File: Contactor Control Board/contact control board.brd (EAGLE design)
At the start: 75.9 x 50.8 mm, 29 parts, among them K1 DS2Y-S-DC5V, Q1 2n2222, Q3 2n2222, Q4 MOSFET-NCHANNELFQP30N06L, U1 LM393AN

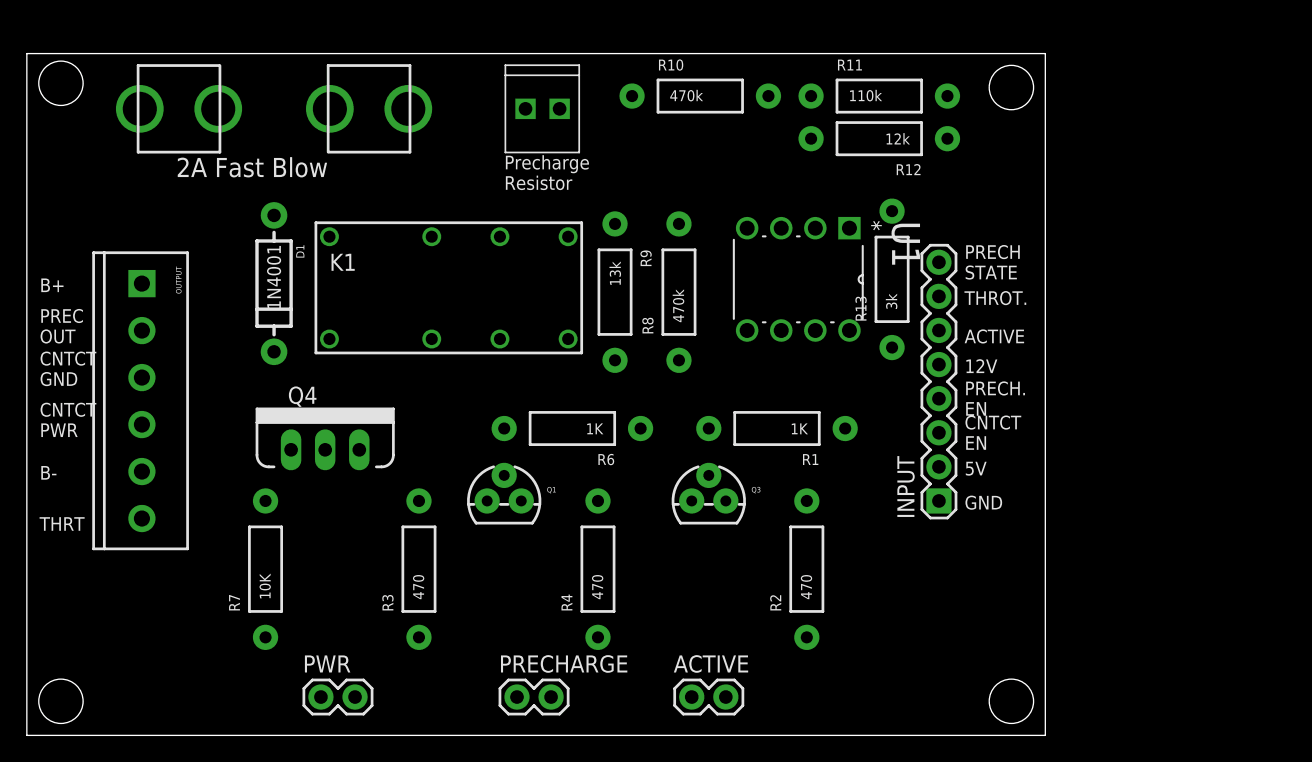
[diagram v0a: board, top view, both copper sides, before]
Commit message: Deleting SMD variant of the CCB for now.
Keeping the two boards in design sync while iterating on one wasn't a
smart idea. Conversion will happen once the CCB has been validated using
proto-boards. Did a test route of the CCB using thru-hole parts in a
2"x3" space and there's a ton of room. Cool!
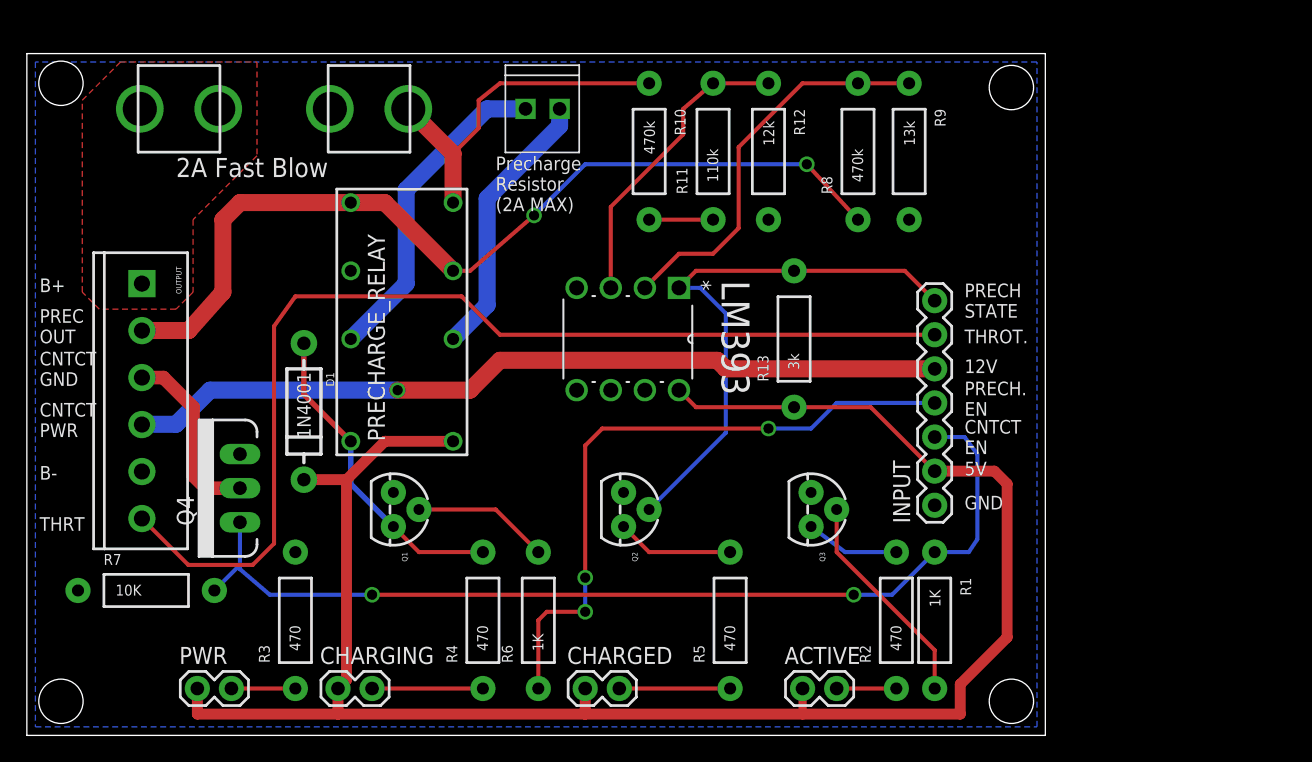
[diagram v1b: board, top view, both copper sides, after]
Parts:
- removed K1: DS2Y-S-DC5V, relay:DS2Y
- removed PRECHARGE: M02PTH, SparkFun-Connectors:1X02
- removed U1: LM393AN, Fairchild_By_element14_Batch_1:DIP254P762X508-8
- added CHARGED, CHARGING: M02PTH, SparkFun-Connectors:1X02
- added LM393: LM393AN, Fairchild_By_element14_Batch_1:DIP254P762X508-8
- added PRECHARGE_RELAY: DS2Y-S-DC5V, relay:DS2Y
- added Q2: 2n2222, SparkFun-DiscreteSemi:TO-92
- added R5: 470, SparkFun-Resistors:AXIAL-0.4
- INPUT: device SparkFun-Connectors:1X08 -> SparkFun-Connectors:1X07
- moved R9 24.3 mm to (65.7, 43.5)
- moved R1 18.5 mm to (67.6, 8.57), turned to 270 degrees
- moved R8 17.0 mm to (61.9, 43.5)
- moved R6 14.5 mm to (38.1, 8.57), turned to 90 degrees
- moved R11 13.1 mm to (51.1, 43.5), turned to 90 degrees
- moved R3 9.96 mm to (20.0, 8.57)
- moved D1 9.78 mm to (20.6, 24.1)
- moved R4 9.38 mm to (34.0, 8.57)
- moved PWR 9.23 mm to (12.7, 3.49)
- moved R7 9.03 mm to (8.89, 10.8), turned to 0 degrees
- moved R13 8.55 mm to (57.1, 29.5)
- moved R12 8.31 mm to (55.2, 43.5), turned to 270 degrees
- moved Q1 8.28 mm to (27.3, 16.8), turned to 270 degrees
- moved ACTIVE 8.28 mm to (57.8, 3.49)
- moved R2 7.68 mm to (64.8, 8.57)
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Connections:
- removed net ACTIVE_LED_EN: INPUT.6, R1.P$1
- new net N$4: CHARGED.2, R5.P$1
- new net N$5: Q2.3, R5.P$2
- net 5V: now also CHARGED.1, CHARGING.1, LM393.8, PRECHARGE_RELAY.1; no longer K1.1, PRECHARGE.1, U1.8
- net 72V_IN_FUSED: now also PRECHARGE_RELAY.8; no longer K1.8
- net CAP_CHARGE_REF: now also LM393.3; no longer U1.3
- net CAP_CHARGE_V_CURR: now also LM393.2; no longer U1.2
- net CONTACT_EN: now also R1.P$1
- net GND: now also LM393.4, PRECHARGE_RELAY.11, Q2.1, R9.P$2; no longer K1.11, U1.4
- net N$14: now also CHARGING.2; no longer PRECHARGE.2
- net PRECHARGE_OUT: now also PRECHARGE_RELAY.6, PRECHARGE_RELAY.9, R8.P$1; no longer K1.6, K1.9, R9.P$2
- net PRECHARGE_RESISTOR_IN: now also PRECHARGE_RELAY.4; no longer K1.4
- net PRECHARGE_RESISTOR_OUT: now also PRECHARGE_RELAY.13; no longer K1.13, R8.P$1
- net PRECH_STATE: now also INPUT.7, LM393.1, Q2.2; no longer INPUT.8, U1.1
- net PRECH_TRAN_COLLECTOR: now also PRECHARGE_RELAY.16; no longer K1.16
- net THROTTLE: now also INPUT.6; no longer INPUT.7
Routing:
- net 5V: track 0.00 -> 138.5 mm
- net THROTTLE: track 0.00 -> 79.7 mm
- net CONTACT_EN: track 0.00 -> 73.8 mm, vias 0 -> 2
- net PRECHARGE_OUT: track 0.00 -> 67.6 mm, vias 0 -> 2
- net 12V: track 0.00 -> 61.3 mm, vias 0 -> 1
- net PRECHARGE_EN: track 0.00 -> 48.6 mm, vias 0 -> 3
- net PRECH_STATE: track 0.00 -> 41.8 mm
- net CAP_CHARGE_V_CURR: track 0.00 -> 29.5 mm
- net 72V_IN_FUSED: track 0.00 -> 26.3 mm
- net PRECHARGE_RESISTOR_OUT: track 0.00 -> 24.2 mm
- net PRECH_TRAN_COLLECTOR: track 0.00 -> 23.9 mm
- net CAP_CHARGE_REF: track 0.00 -> 22.6 mm
- net PRECHARGE_RESISTOR_IN: track 0.00 -> 20.4 mm
- net N$2: track 0.00 -> 16.4 mm
- net CONTACT_GND: track 0.00 -> 13.7 mm
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- added copper zone on layer 1, net 72V_IN
- added copper zone on layer 16, net GND
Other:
- board text added: "Precharge Resistor (2A MAX)"
- board text removed: "ACTIVE"
- board text removed: "Precharge Resistor"

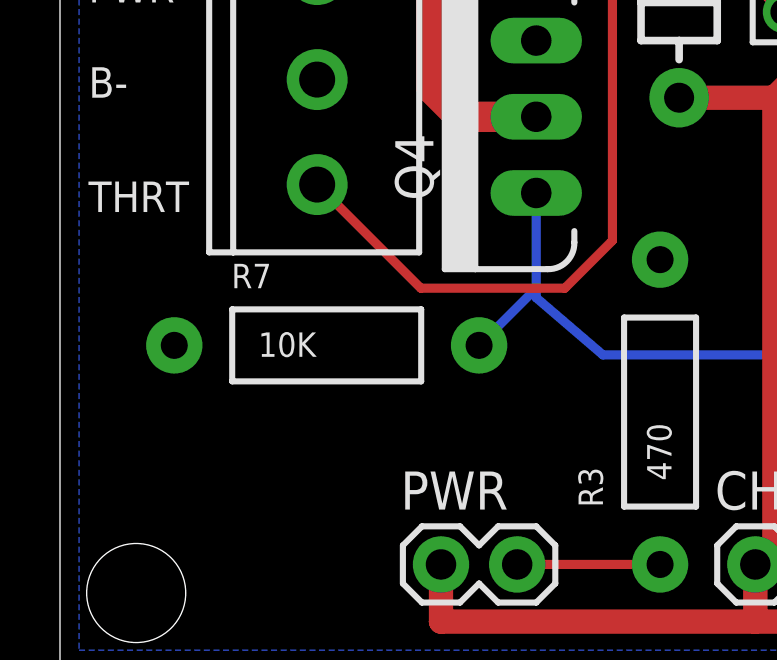
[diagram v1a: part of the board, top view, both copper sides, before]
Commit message: Added BMS interface board and updated CCB with current limiting resistor
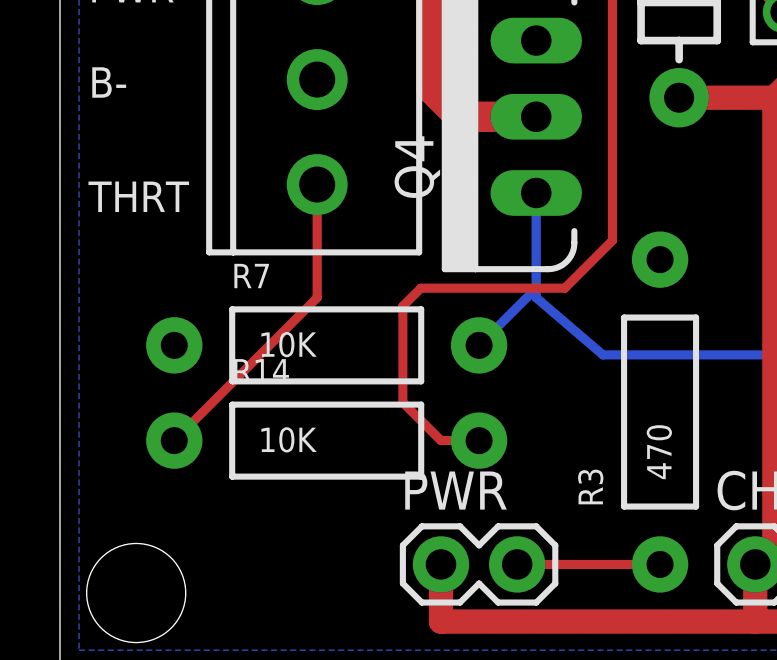
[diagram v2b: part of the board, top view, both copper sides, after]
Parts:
- added R14: 10K, SparkFun-Resistors:AXIAL-0.4
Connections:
- new net THROTTLE_CURRENT_LIMITED: OUTPUT.6, R14.P$1
- net THROTTLE: now also R14.P$2; no longer OUTPUT.6
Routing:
- net THROTTLE_CURRENT_LIMITED: track 0.00 -> 10.5 mm
- net THROTTLE: track 79.7 -> 81.9 mm
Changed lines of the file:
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@@
 <setting verticaltext="up"/>
 </settings>
-<grid distance="0.0125" unitdist="inch" unit="inch" style="lines" multiple="1" display="yes" altdistance="0.005" altunitdist="inch" altunit="inch"/>
+<grid distance="0.05" unitdist="inch" unit="inch" style="lines" multiple="1" display="yes" altdistance="0.005" altunitdist="inch" altunit="inch"/>
 <layers>
 <layer number="1" name="Top" color="4" fill="1" visible="yes" active="yes"/>
@@
 <element name="Q2" library="SparkFun-DiscreteSemi" package="TO-92" value="2n2222" x="44.45" y="16.8275" rot="R270"/>
 <element name="R5" library="SparkFun-Resistors" package="AXIAL-0.4" value="470" x="52.3875" y="8.5725" rot="R90"/>
+<element name="R14" library="SparkFun-Resistors" package="AXIAL-0.4" value="10K" x="8.89" y="7.62"/>
 </elements>
 <signals>
@@
 </signal>
 <signal name="THROTTLE">
-<contactref element="OUTPUT" pad="6"/>
 <contactref element="INPUT" pad="6"/>
 <wire x1="67.6275" y1="29.845" x2="35.2425" y2="29.845" width="0.3048" layer="1"/>
@@
 <wire x1="18.415" y1="14.2875" x2="16.8275" y2="12.7" width="0.3048" layer="1"/>
 <wire x1="16.8275" y1="12.7" x2="12.0275" y2="12.7" width="0.3048" layer="1"/>
-<wire x1="12.0275" y1="12.7" x2="8.5725" y2="16.155" width="0.3048" layer="1"/>
+<contactref element="R14" pad="P$2"/>
+<wire x1="12.0275" y1="12.7" x2="11.43" y2="12.1025" width="0.3048" layer="1"/>
+<wire x1="11.43" y1="12.1025" x2="11.43" y2="8.89" width="0.3048" layer="1"/>
+<wire x1="11.43" y1="8.89" x2="12.7" y2="7.62" width="0.3048" layer="1"/>
+<wire x1="12.7" y1="7.62" x2="13.97" y2="7.62" width="0.3048" layer="1"/>
 </signal>
 <signal name="72V_IN">
@@
 <wire x1="46.355" y1="13.6525" x2="52.3875" y2="13.6525" width="0.3048" layer="1"/>
 </signal>
+<signal name="THROTTLE_CURRENT_LIMITED">
+<contactref element="OUTPUT" pad="6"/>
+<contactref element="R14" pad="P$1"/>
+<wire x1="3.81" y1="7.62" x2="8.5725" y2="12.3825" width="0.3048" layer="1"/>
+<wire x1="8.5725" y1="12.3825" x2="8.5725" y2="16.155" width="0.3048" layer="1"/>
+</signal>
 </signals>

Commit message: Opto-coupling precharge signal with op-amp output
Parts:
- added C1: 0.1uF, SparkFun-Capacitors:0603-CAP
- added OK2: 6N138, optocoupler:DIL08
- added R15: 470, SparkFun-Resistors:AXIAL-0.4
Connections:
- new net PRECH_STATE_TO_OPTO: LM393.1, OK2.2, R13.P$2
- net 5V: now also C1.1, OK2.8, R15.P$1
- net GND: now also C1.2, OK2.3, OK2.5
- net PRECH_STATE: now also OK2.6, R15.P$2; no longer LM393.1, R13.P$2
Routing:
- net PRECH_STATE: track 41.8 -> 22.8 mm
- net PRECH_STATE_TO_OPTO: track 0.00 -> 9.10 mm
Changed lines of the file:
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@@
 <layer number="23" name="tOrigins" color="15" fill="1" visible="yes" active="yes"/>
 <layer number="24" name="bOrigins" color="15" fill="1" visible="yes" active="yes"/>
-<layer number="25" name="tNames" color="16" fill="1" visible="yes" active="yes"/>
+<layer number="25" name="tNames" color="16" fill="1" visible="no" active="yes"/>
 <layer number="26" name="bNames" color="16" fill="1" visible="no" active="yes"/>
 <layer number="27" name="tValues" color="7" fill="1" visible="no" active="yes"/>
@@
 <element name="R5" library="SparkFun-Resistors" package="AXIAL-0.4" value="470" x="52.3875" y="8.5725" rot="R90"/>
 <element name="R14" library="SparkFun-Resistors" package="AXIAL-0.4" value="10K" x="8.89" y="7.62"/>
+<element name="C1" library="SparkFun-Capacitors" package="0603-CAP" value="0.1uF" x="83.82" y="29.21"/>
+<element name="R15" library="SparkFun-Resistors" package="AXIAL-0.4" value="470" x="87.63" y="35.56"/>
+<element name="OK2" library="optocoupler" package="DIL08" value="6N138" x="86.36" y="46.99" rot="R180">
+<attribute name="OC_NEWARK" value="35K5294" x="86.36" y="46.99" size="1.778" layer="27" ratio="15" rot="R180" display="off"/>
+<attribute name="MPN" value="6N138" x="86.36" y="46.99" size="1.778" layer="27" ratio="15" rot="R180" display="off"/>
+<attribute name="MF" value="VISHAY/TELEFUNKEN" x="86.36" y="46.99" size="1.778" layer="27" ratio="15" rot="R180" display="off"/>
+<attribute name="OC_FARNELL" value="9860150" x="86.36" y="46.99" size="1.778" layer="27" ratio="15" rot="R180" display="off"/>
+</element>
 </elements>
 <signals>
@@
 <wire x1="23.8125" y1="19.05" x2="23.8125" y2="4.1275" width="0.8128" layer="1"/>
 <wire x1="23.8125" y1="4.1275" x2="23.1775" y2="3.4925" width="0.8128" layer="1"/>
+<contactref element="C1" pad="1"/>
+<contactref element="R15" pad="P$1"/>
+<contactref element="OK2" pad="8"/>
+<wire x1="82.97" y1="29.21" x2="90.17" y2="43.18" width="0" layer="19" extent="1-1"/>
+<wire x1="82.55" y1="35.56" x2="82.97" y2="29.21" width="0" layer="19" extent="1-1"/>
+<wire x1="12.7" y1="1.5875" x2="82.97" y2="29.21" width="0" layer="19" extent="1-1"/>
 </signal>
 <signal name="GND">
@@
 </polygon>
 <contactref element="R9" pad="P$2"/>
+<contactref element="OK2" pad="3"/>
+<contactref element="C1" pad="2"/>
+<contactref element="OK2" pad="5"/>
+<wire x1="55.245" y1="38.4175" x2="65.7225" y2="38.4175" width="0" layer="19" extent="1-1"/>
+<wire x1="40.9575" y1="33.3375" x2="55.245" y2="38.4175" width="0" layer="19" extent="1-1"/>
+<wire x1="44.45" y1="18.0975" x2="40.9575" y2="33.3375" width="0" layer="19" extent="1-1"/>
+<wire x1="58.42" y1="18.0975" x2="44.45" y2="18.0975" width="0" layer="19" extent="1-1"/>
+<wire x1="67.6275" y1="17.145" x2="58.42" y2="18.0975" width="0" layer="19" extent="1-1"/>
+<wire x1="24.13" y1="34.6075" x2="40.9575" y2="33.3375" width="0" layer="19" extent="1-1"/>
+<wire x1="15.875" y1="20.955" x2="24.13" y2="34.6075" width="0" layer="19" extent="1-1"/>
+<wire x1="8.5725" y1="19.655" x2="15.875" y2="20.955" width="0" layer="19" extent="1-1"/>
+<wire x1="20.0025" y1="13.6525" x2="15.875" y2="20.955" width="0" layer="19" extent="1-1"/>
+<wire x1="27.305" y1="18.0975" x2="20.0025" y2="13.6525" width="0" layer="19" extent="1-1"/>
+<wire x1="3.81" y1="10.795" x2="8.5725" y2="19.655" width="0" layer="19" extent="1-1"/>
+<wire x1="84.67" y1="29.21" x2="3.81" y2="10.795" width="0" layer="19" extent="1-1"/>
+<wire x1="82.55" y1="43.18" x2="84.67" y2="29.21" width="0" layer="19" extent="1-1"/>
+<wire x1="85.09" y1="50.8" x2="84.67" y2="29.21" width="0" layer="19" extent="1-1"/>
 </signal>
 <signal name="CONTACT_EN">
@@
 </signal>
 <signal name="PRECH_STATE">
-<contactref element="R13" pad="P$2"/>
-<contactref element="LM393" pad="1"/>
 <contactref element="INPUT" pad="7"/>
 <contactref element="Q2" pad="2"/>
-<wire x1="57.15" y1="34.6075" x2="65.405" y2="34.6075" width="0.3048" layer="1"/>
 <wire x1="65.405" y1="34.6075" x2="67.6275" y2="32.385" width="0.3048" layer="1"/>
-<wire x1="57.15" y1="34.6075" x2="49.8475" y2="34.6075" width="0.3048" layer="1"/>
-<wire x1="49.8475" y1="34.6075" x2="48.5775" y2="33.3375" width="0.3048" layer="1"/>
-<wire x1="48.5775" y1="33.3375" x2="50.165" y2="33.3375" width="0.3048" layer="16"/>
 <wire x1="50.165" y1="33.3375" x2="52.07" y2="31.4325" width="0.3048" layer="16"/>
 <wire x1="52.07" y1="31.4325" x2="52.07" y2="22.5425" width="0.3048" layer="16"/>
 <wire x1="52.07" y1="22.5425" x2="46.355" y2="16.8275" width="0.3048" layer="16"/>
+<contactref element="R15" pad="P$2"/>
+<contactref element="OK2" pad="6"/>
+<wire x1="52.07" y1="31.4325" x2="65.405" y2="34.6075" width="0" layer="19" extent="1-16"/>
+<wire x1="92.71" y1="35.56" x2="46.355" y2="16.8275" width="0" layer="19" extent="1-1"/>
+<wire x1="85.09" y1="43.18" x2="92.71" y2="35.56" width="0" layer="19" extent="1-1"/>
 </signal>
 <signal name="CAP_CHARGE_REF">
@@
 <wire x1="8.5725" y1="12.3825" x2="8.5725" y2="16.155" width="0.3048" layer="1"/>
 </signal>
+<signal name="PRECH_STATE_TO_OPTO">
+<contactref element="R13" pad="P$2"/>
+<contactref element="LM393" pad="1"/>
+<wire x1="57.15" y1="34.6075" x2="49.8475" y2="34.6075" width="0.3048" layer="1"/>
+<wire x1="49.8475" y1="34.6075" x2="48.5775" y2="33.3375" width="0.3048" layer="1"/>
+<contactref element="OK2" pad="2"/>
+<wire x1="87.63" y1="50.8" x2="48.5775" y2="33.3375" width="0" layer="19" extent="1-1"/>
+</signal>
 </signals>
